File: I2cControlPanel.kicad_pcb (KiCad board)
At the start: 2 copper layers, 100 x 100 mm, 61 parts, among them J1 JoystickL, J2 Conn_01x06, J3 Conn_01x04, J4 Conn_01x04, J5 JoystickR, J6 Conn_01x04, SW6 SW_Push, U1 NJM12888F33, U2 ATmega328PB-MU, U3 AQM0802

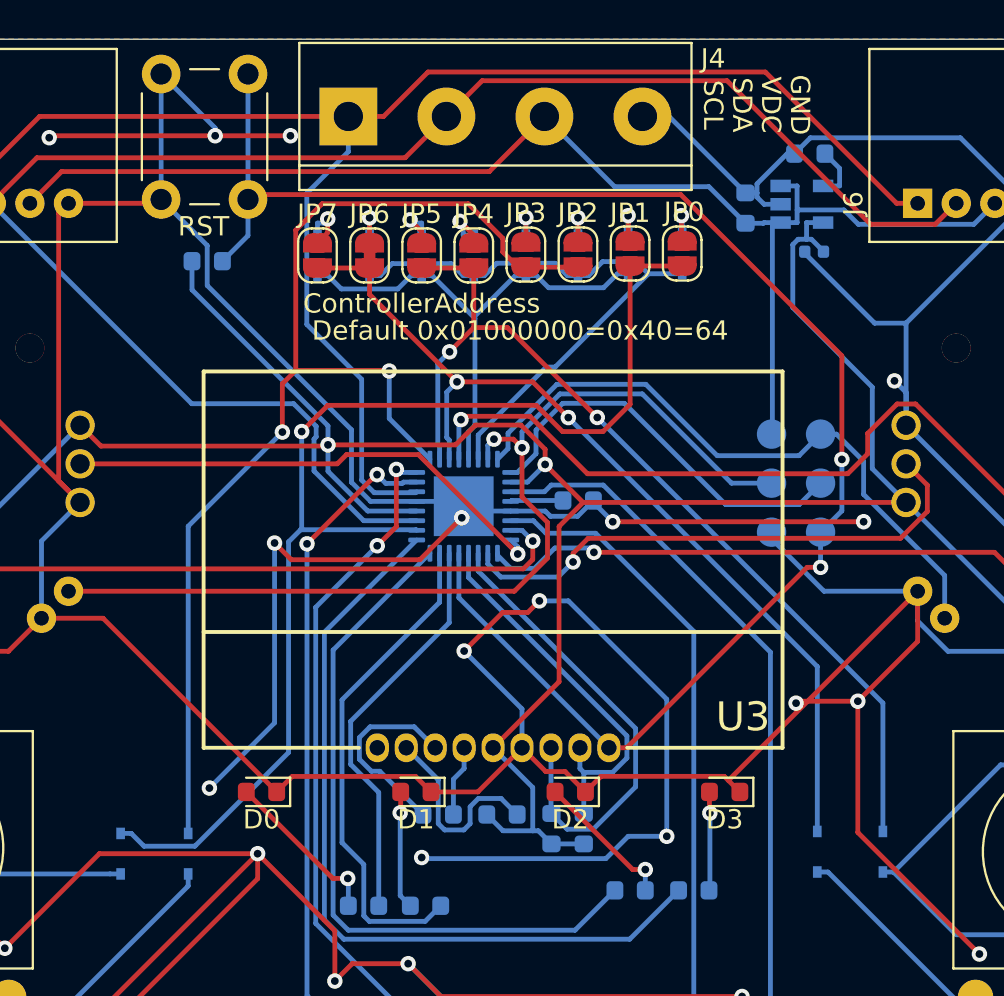
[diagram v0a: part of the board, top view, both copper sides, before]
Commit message: Change pad for diode
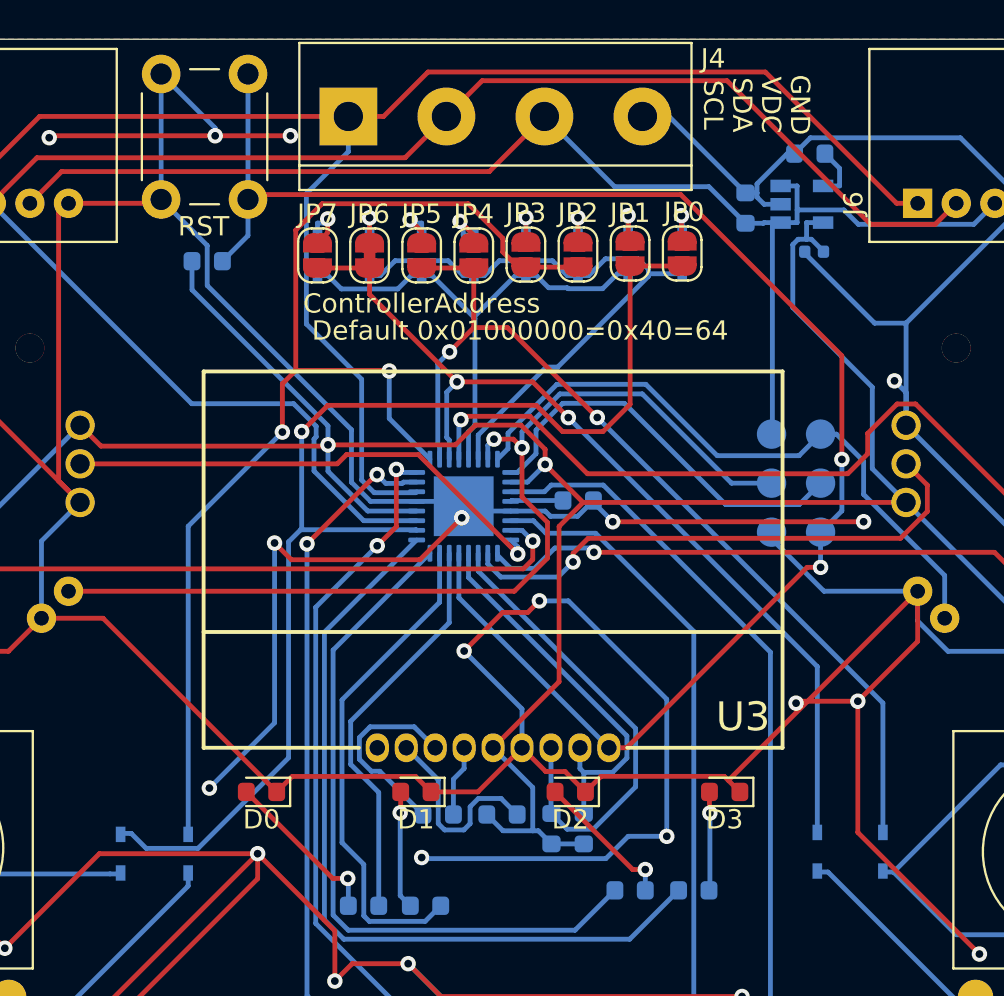
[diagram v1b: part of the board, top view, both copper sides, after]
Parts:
- D10, D11, D12, D13, D14, D15, D4, D5, D6, D7, D8, D9: footprint Diode_SMD:D_SOD-323 -> my-kicad-footprints:D_SOD-523F
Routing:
- net /BtnSig2: track 31.3 -> 31.9 mm

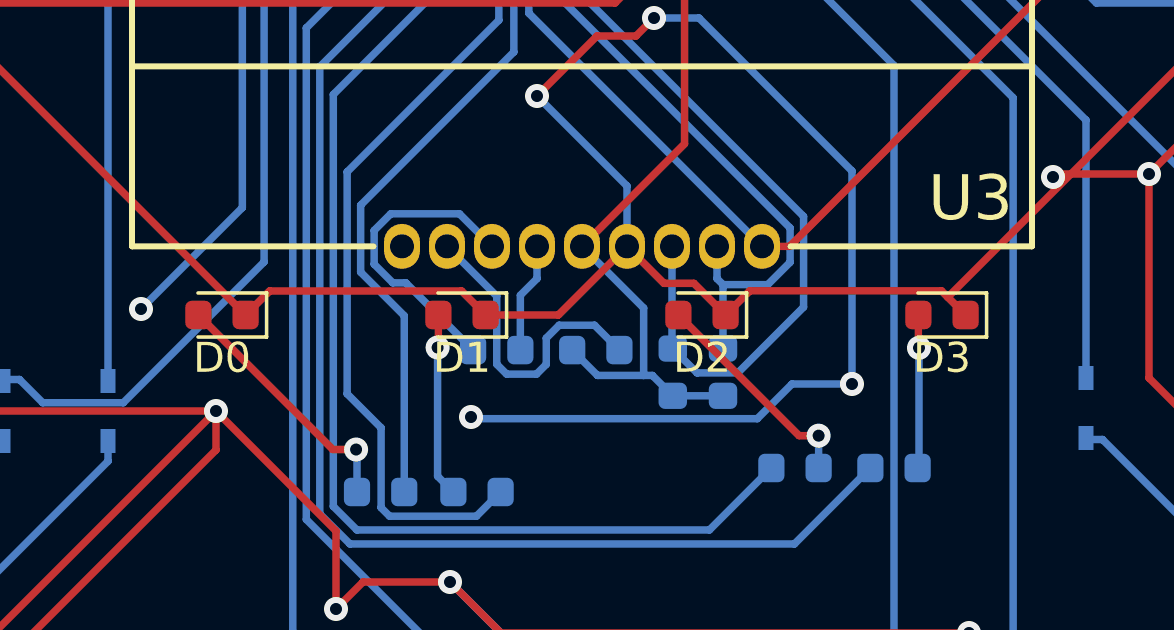
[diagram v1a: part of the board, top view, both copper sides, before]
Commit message: Update pad of led for soldering by hand
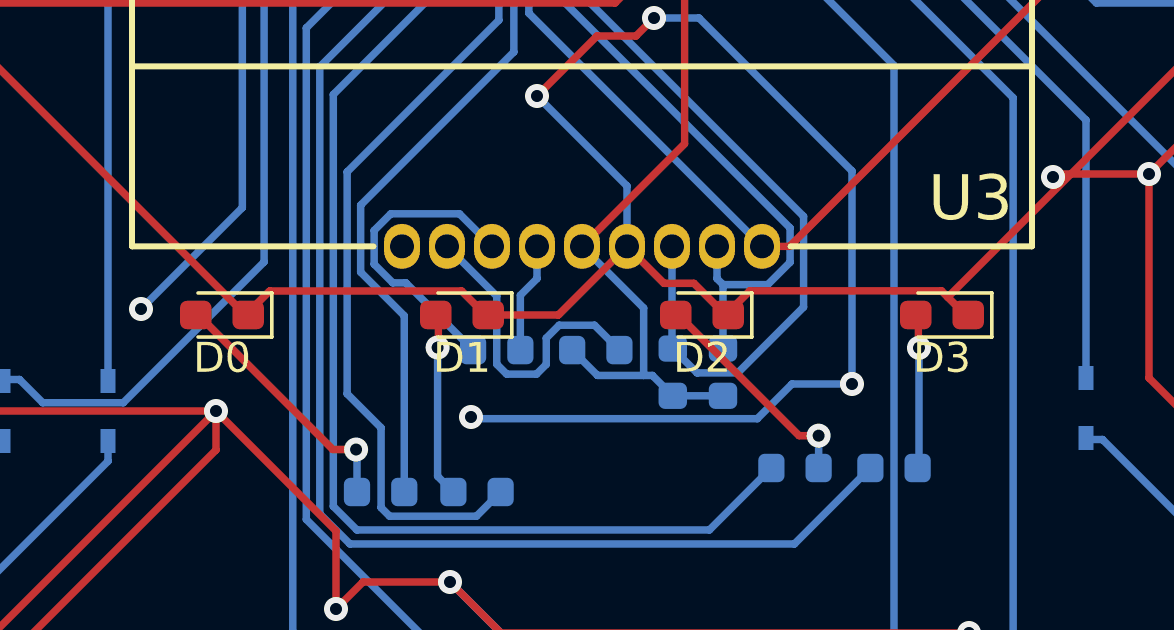
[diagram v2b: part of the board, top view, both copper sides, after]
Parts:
- D0, D1, D2, D3: footprint Diode_SMD:D_0603_1608Metric -> Diode_SMD:D_0603_1608Metric_Pad1.05x0.95mm_HandSolder

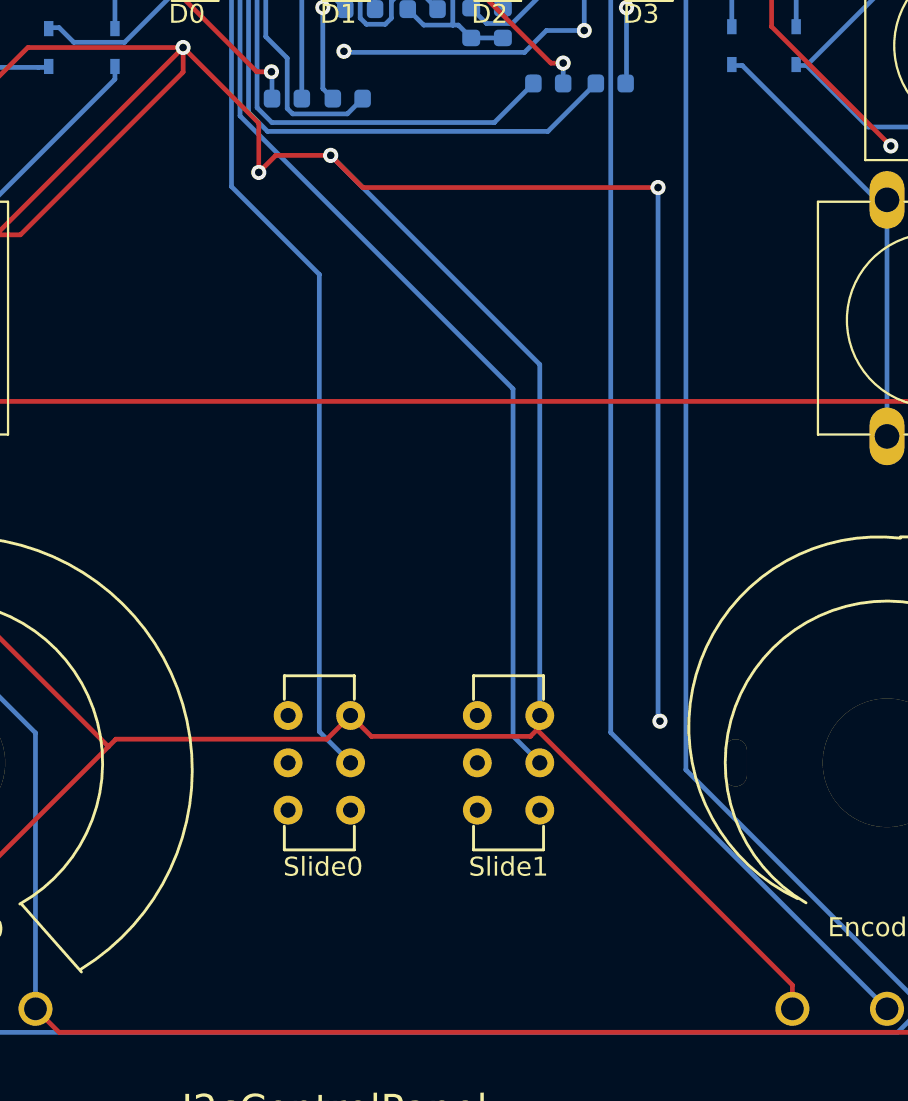
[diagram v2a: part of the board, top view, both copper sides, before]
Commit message: Change slide switch
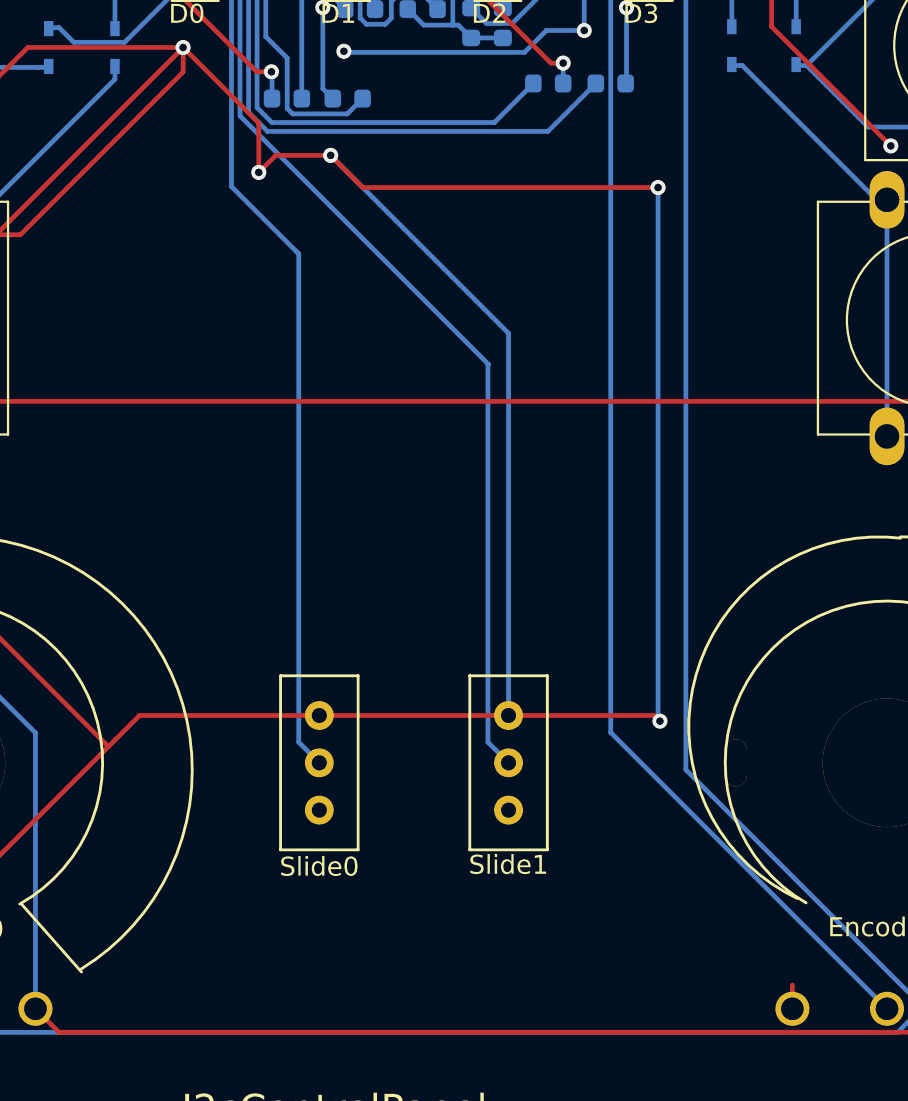
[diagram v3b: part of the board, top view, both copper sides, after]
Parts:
- Slide0, Slide1: footprint my-kicad-footprints:SlideSwitch -> my-kicad-footprints:SlideSwitch_SS12D01G4_2posi_1line
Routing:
- net GND: track 923.1 -> 908.5 mm
- net /Slide0: track 63.8 -> 63.2 mm
- net /Slide1: track 67.1 -> 66.5 mm

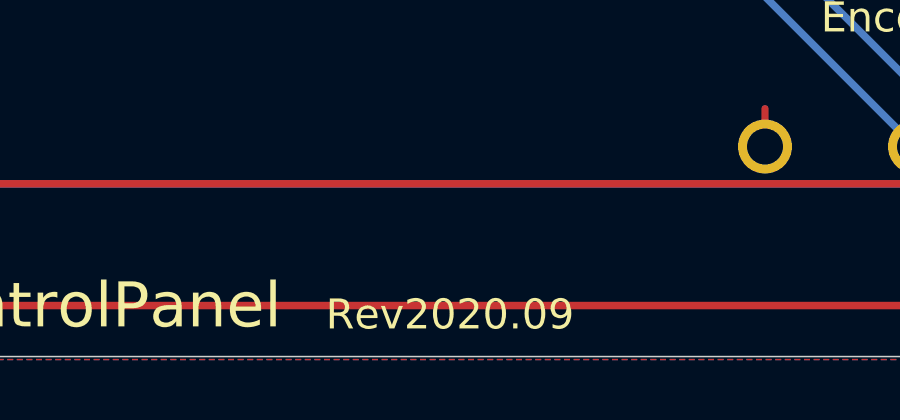
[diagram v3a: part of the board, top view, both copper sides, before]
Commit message: Update revision to 2020.10
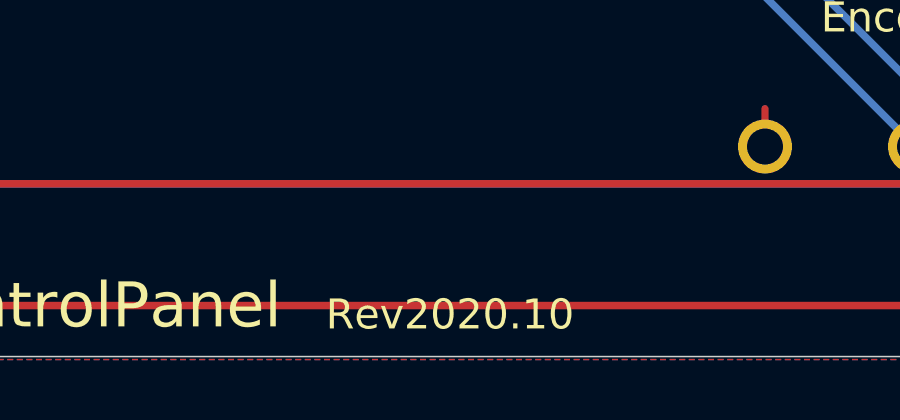
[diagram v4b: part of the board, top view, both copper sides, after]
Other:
- board text added: "Rev2020.10"
- board text removed: "Rev2020.09"
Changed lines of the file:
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@@
   (gr_arc (start 54 146) (end 54 150) (angle 90) (layer Edge.Cuts) (width 0.05))
   (gr_arc (start 54 54) (end 50 54) (angle 90) (layer Edge.Cuts) (width 0.05))
-  (gr_text Rev2020.09 (at 109.5 148.6) (layer F.SilkS)
+  (gr_text Rev2020.10 (at 109.5 148.6) (layer F.SilkS)
     (effects (font (size 1 1) (thickness 0.15)))
   )

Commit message: Add size info to pcb
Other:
- board text added: "4.3mm for M4"

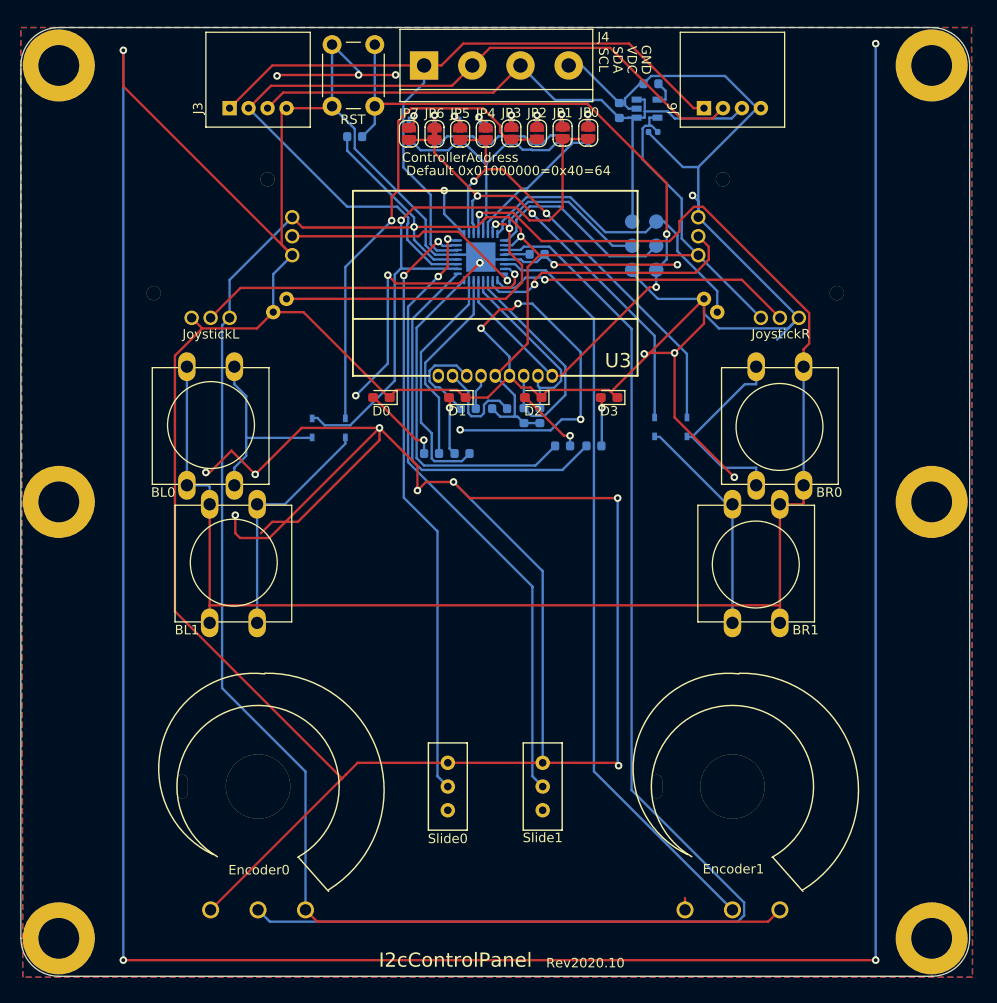
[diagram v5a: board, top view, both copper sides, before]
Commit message: Use diode array and add mounting holes as Rev2021.03
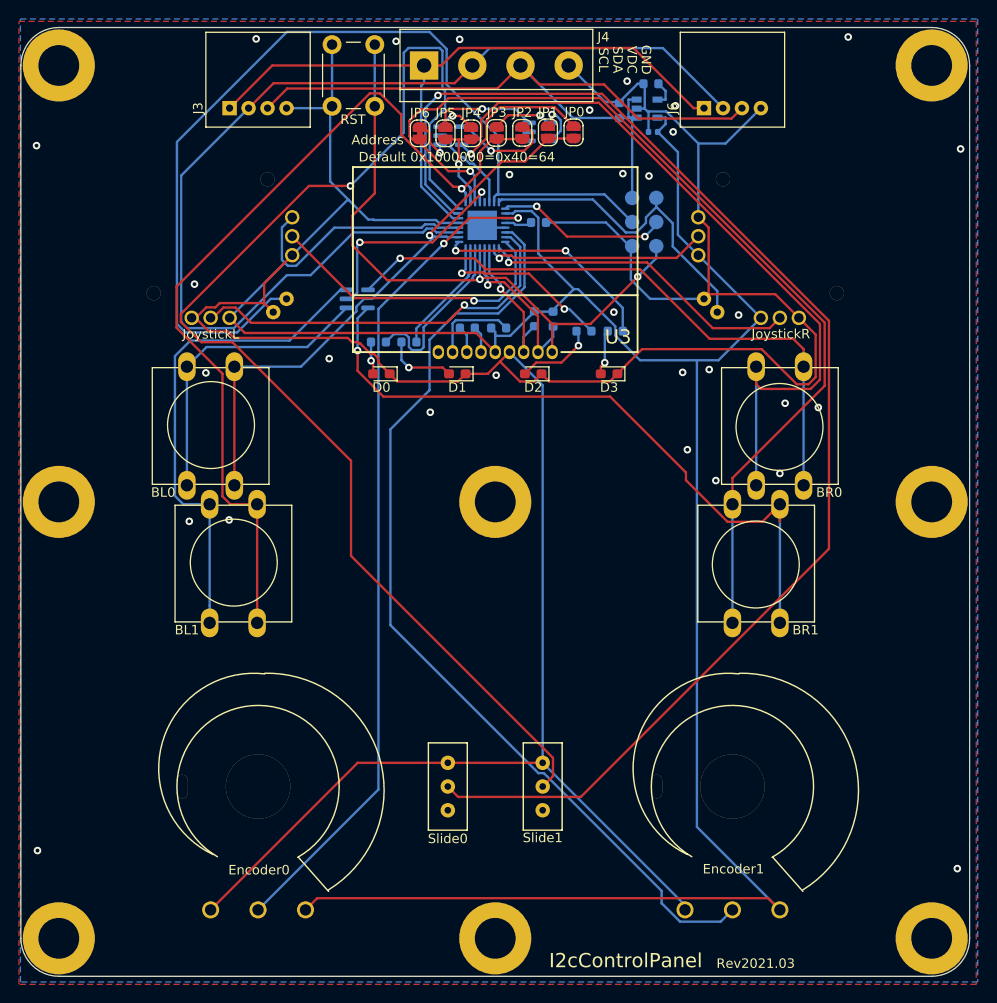
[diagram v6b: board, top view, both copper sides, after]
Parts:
- removed D10, D11, D12, D13, D14, D15, D7, D8, D9: D, my-kicad-footprints:D_SOD-523F
- removed JP7: NO, Jumper:SolderJumper-2_P1.3mm_Open_RoundedPad1.0x1.5mm
- removed R7: 10k, Resistor_SMD:R_0603_1608Metric
- added REF7: MountingHole_4.3mm_M4_ISO7380_Pad, MountingHole:MountingHole_4.3mm_M4_ISO7380_Pad, F.Cu at (100.0, 100.0)
- added REF8: MountingHole_4.3mm_M4_ISO7380_Pad, MountingHole:MountingHole_4.3mm_M4_ISO7380_Pad, F.Cu at (100.0, 146.0)
- D4, D5, D6: value D -> 1SS309; footprint my-kicad-footprints:D_SOD-523F -> my-kicad-footprints:SC-74-5_1.6x2.9mm_P0.95mm
- R1, R2, R3, R4: value 1k -> 10k
- moved D6 20.5 mm to (85.5, 78.6), turned to 0 degrees
- moved R1 13.0 mm to (87.7, 83.2)
- moved R2 13.0 mm to (90.9, 83.2)
- moved R3 12.3 mm to (109.3, 82.0), turned to 180 degrees
- moved R4 12.3 mm to (112.7, 82.0), turned to 180 degrees
- moved D5 11.1 mm to (104.7, 61.0), turned to 0 degrees
- moved R5 10.3 mm to (104.1, 80.7), turned to 270 degrees
- moved R6 10.3 mm to (106.1, 80.7), turned to 270 degrees
- moved C5 8.50 mm to (100.4, 81.7)
- moved C6 8.50 mm to (97.1, 81.7)
- moved D4 4.42 mm to (95.3, 61.4), turned to 0 degrees
- moved C4 3.35 mm to (104.6, 70.5)
- moved U2 3.35 mm to (98.6, 70.8)
- moved D0 2.50 mm to (88.0, 86.5)
- moved D1 2.50 mm to (96.0, 86.5)
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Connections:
- BL0 pad 1: /BtnSig0 -> Net-(BL0-Pad1)
- BL0 pad 2: Net-(BL0-Pad2) -> /BTN0
- BL1 pad 1: /BtnSig0 -> Net-(BL1-Pad1)
- BL1 pad 2: Net-(BL1-Pad2) -> /BTN1
- BR0 pad 1: /BtnSig0 -> Net-(BR0-Pad1)
- BR0 pad 2: Net-(BR0-Pad2) -> /BTN2
- BR1 pad 1: /BtnSig0 -> Net-(BR1-Pad1)
- BR1 pad 2: Net-(BR1-Pad2) -> /BTN3
- D4 pad 1: /BtnSig1 -> Net-(D4-Pad1)
- D4 pad 2: Net-(D4-Pad2) -> /BtnSig2
- D5 pad 1: /BtnSig2 -> Net-(D5-Pad1)
- D6 pad 1: /BtnSig1 -> Net-(BL0-Pad1)
- D6 pad 2: Net-(D6-Pad2) -> /BtnSig0
- JP0 pad 2: Net-(D11-Pad2) -> Net-(D4-Pad5)
- JP1 pad 2: Net-(D10-Pad2) -> Net-(D5-Pad5)
- JP2 pad 2: Net-(D9-Pad2) -> Net-(D4-Pad4)
- JP3 pad 2: Net-(D8-Pad2) -> Net-(D5-Pad4)
- JP4 pad 2: Net-(D7-Pad2) -> Net-(D4-Pad3)
- JP5 pad 2: Net-(D6-Pad2) -> Net-(D5-Pad3)
- JP6 pad 2: Net-(D5-Pad2) -> Net-(D4-Pad1)
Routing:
- net GND: track 908.5 -> 335.3 mm, vias 28 -> 31
- net /BtnSig0: track 169.6 -> 23.1 mm, vias 1 -> 2
- net /Slide0: track 63.2 -> 141.4 mm, vias 2 -> 1
- net Net-(BR1-Pad1): track 0.00 -> 73.8 mm, vias 0 -> 1
- net Net-(BR0-Pad1): track 0.00 -> 65.6 mm, vias 0 -> 1
- net /Slide1: track 66.5 -> 131.4 mm, vias 2 -> 1
- net /BTN3: track 48.1 -> 103.6 mm, vias 2 -> 1
- net Net-(BL1-Pad1): track 0.00 -> 52.2 mm
- net /JoyBtnL: track 51.1 -> 100.5 mm, vias 2 -> 0
- net /Rotery1: track 135.9 -> 88.7 mm, vias 0 -> 2
- net /BTN2: track 49.3 -> 86.6 mm, vias 2 -> 1
- net /BTN1: track 61.0 -> 96.0 mm, vias 2 -> 1
- net Net-(BL0-Pad1): track 0.00 -> 31.9 mm
- net /SDA: track 86.5 -> 114.8 mm
- net /BtnSig1: track 26.6 -> 0.00 mm
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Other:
- board text added: "Address"
- board text added: "Default 0x1000000=0x40=64"
- board text added: "Rev2021.03"
- board text removed: "ControllerAddress"
- board text removed: "Default 0x01000000=0x40=64"
- board text removed: "Rev2020.10"

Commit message: Update pcb for Rev2021.04
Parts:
- C1, C4, C5, C6: footprint Capacitor_SMD:C_0603_1608Metric -> Capacitor_SMD:C_0402_1005Metric
- J1, J5: footprint my-kicad-footprints:LowHeightJoyStickWithButton -> my-kicad-footprints:PS4tJoystick
- moved C4 0.34 mm to (104.2, 70.6)
- turned J1 to 90 degrees
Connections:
- J1 pad 1: +3V3 -> GND
- J1 pad 3: GND -> +3V3
- J5 pad 1: GND -> +3V3
- J5 pad 2: /VertValueR -> /HoriValueR
- J5 pad 3: +3V3 -> GND
- J5 pad 4: +3V3 -> GND
- J5 pad 5: /HoriValueR -> /VertValueR
- J5 pad 6: GND -> +3V3
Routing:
- net /Slide0: track 141.4 -> 68.0 mm, vias 1 -> 0
- net /Rotery1: track 88.7 -> 141.3 mm, vias 2 -> 1
- net /Slide1: track 131.4 -> 81.7 mm, vias 1 -> 0
- net GND: track 335.3 -> 292.8 mm, vias 31 -> 25
- net /BTN0: track 62.1 -> 101.9 mm
- net /JoyBtnL: track 100.5 -> 66.1 mm
- net +3V3: track 254.3 -> 287.2 mm, vias 0 -> 2
- net /SDA: track 114.8 -> 83.4 mm, vias 0 -> 1
- net /BTN1: track 96.0 -> 66.5 mm
- net /BTN2: track 86.6 -> 110.2 mm
- net /BTN3: track 103.6 -> 125.8 mm
- net /Rotery2: track 101.4 -> 81.7 mm
- net /JoyBtnR: track 34.3 -> 53.8 mm, vias 0 -> 1
- net VDC: track 80.5 -> 66.2 mm
- net /HoriValueR: track 23.4 -> 35.7 mm
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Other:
- board text added: "Rev2021.04"
- board text removed: "Rev2021.03"
